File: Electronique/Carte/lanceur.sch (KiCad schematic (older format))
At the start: 4 parts, among them P4 CONN_jacky_led, P5 CONN_LED, Q1 IRF540N, U9 MC34152

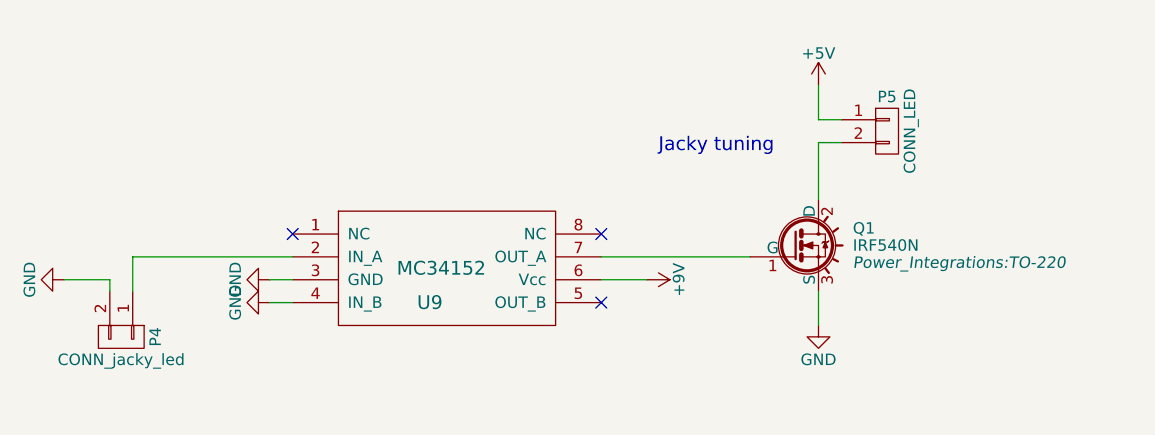
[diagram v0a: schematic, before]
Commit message: rapide corretion des empreintes pour les servos
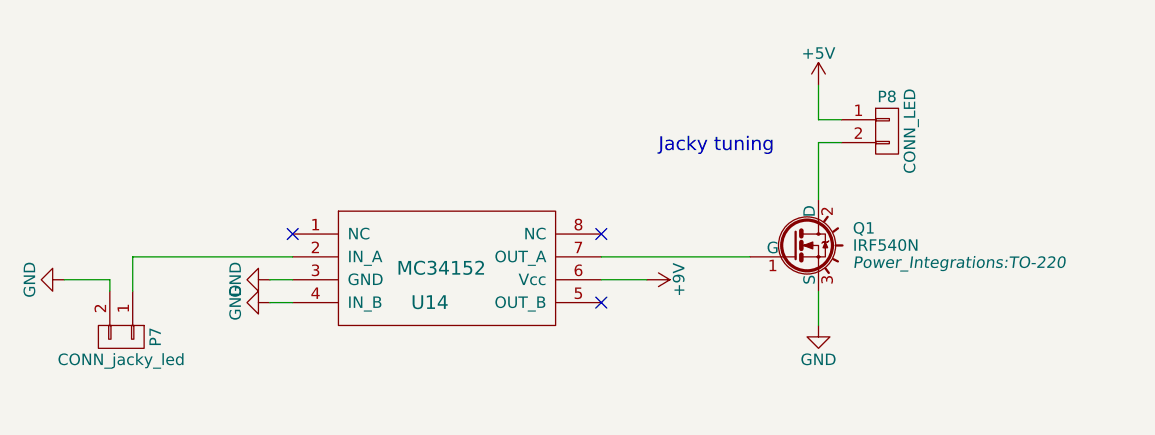
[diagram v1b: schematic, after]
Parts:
- renumbered P4 to P7, P5 to P8, U9 to U14
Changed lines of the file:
@@
 Jacky tuning
 $Comp
-L MC34152 U9
+L MC34152 U14
 U 1 1 5A767332
 P 4600 3900
-F 0 "U9" H 4600 4000 60  0000 C CNN
+F 0 "U14" H 4600 4000 60  0000 C CNN
 F 1 "MC34152" H 4650 4150 60  0000 C CNN
 F 2 "Housings_DIP:DIP-8_W7.62mm_LongPads" H 4600 3900 60  0001 C CNN
@@
 NoConn ~ 5350 3800
 $Comp
-L GND #PWR049
+L GND #PWR26
 U 1 1 5A767FBA
 P 3900 3800
-F 0 "#PWR049" H 3900 3550 50  0001 C CNN
+F 0 "#PWR26" H 3900 3550 50  0001 C CNN
 F 1 "GND" H 3900 3650 50  0000 C CNN
 F 2 "" H 3900 3800 50  0000 C CNN
@@
 $EndComp
 $Comp
-L GND #PWR050
+L GND #PWR25
 U 1 1 5A767FD6
 P 3900 3700
-F 0 "#PWR050" H 3900 3450 50  0001 C CNN
+F 0 "#PWR25" H 3900 3450 50  0001 C CNN
 F 1 "GND" H 3900 3550 50  0000 C CNN
 F 2 "" H 3900 3700 50  0000 C CNN
@@
 	5350 3600 6000 3600
 $Comp
-L CONN_01X02 P4
+L CONN_01X02 P7
 U 1 1 5A76819E
 P 3250 3950
-F 0 "P4" H 3250 4100 50  0000 C CNN
+F 0 "P7" H 3250 4100 50  0000 C CNN
 F 1 "CONN_jacky_led" V 3350 3950 50  0000 C CNN
 F 2 "Connectors_Molex:Molex_KK-6410-02_02x2.54mm_Straight" H 3250 3950 50  0001 C CNN
@@
 	3300 3600 4000 3600
 $Comp
-L GND #PWR051
+L GND #PWR24
 U 1 1 5A768319
 P 3000 3700
-F 0 "#PWR051" H 3000 3450 50  0001 C CNN
+F 0 "#PWR24" H 3000 3450 50  0001 C CNN
 F 1 "GND" H 3000 3550 50  0000 C CNN
 F 2 "" H 3000 3700 50  0000 C CNN
@@
 	3200 3700 3200 3750
 $Comp
-L GND #PWR052
+L GND #PWR29
 U 1 1 5A7685B8
 P 6300 3900
-F 0 "#PWR052" H 6300 3650 50  0001 C CNN
+F 0 "#PWR29" H 6300 3650 50  0001 C CNN
 F 1 "GND" H 6300 3750 50  0000 C CNN
 F 2 "" H 6300 3900 50  0000 C CNN
@@
 	6300 3750 6300 3900
 $Comp
-L CONN_01X02 P5
+L CONN_01X02 P8
 U 1 1 5A76883C
 P 6600 3050
-F 0 "P5" H 6600 3200 50  0000 C CNN
+F 0 "P8" H 6600 3200 50  0000 C CNN
 F 1 "CONN_LED" V 6700 3050 50  0000 C CNN
 F 2 "Connectors_Molex:Molex_KK-6410-02_02x2.54mm_Straight" H 6600 3050 50  0001 C CNN
@@
 $EndComp
 $Comp
-L +5V #PWR053
+L +5V #PWR28
 U 1 1 5A768873
 P 6300 2850
-F 0 "#PWR053" H 6300 2700 50  0001 C CNN
+F 0 "#PWR28" H 6300 2700 50  0001 C CNN
 F 1 "+5V" H 6300 2990 50  0000 C CNN
 F 2 "" H 6300 2850 50  0000 C CNN
@@
 	6300 3100 6300 3350
 $Comp
-L +9V #PWR054
+L +9V #PWR27
 U 1 1 5ABD7B5A
 P 5550 3700
-F 0 "#PWR054" H 5550 3550 50  0001 C CNN
+F 0 "#PWR27" H 5550 3550 50  0001 C CNN
 F 1 "+9V" H 5550 3840 50  0000 C CNN
 F 2 "" H 5550 3700 50  0000 C CNN

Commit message: correction
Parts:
- removed P7: CONN_jacky_led, Connectors_Molex:Molex_KK-6410-02_02x2.54mm_Straight, symbol CONN_01X02
- removed P8: CONN_LED, Connectors_Molex:Molex_KK-6410-02_02x2.54mm_Straight, symbol CONN_01X02
- added D11: D, Diodes_SMD:D_SMA_Handsoldering, symbol D
- added J8: Conn_01x02, dsn2596:B plug 5mm, symbol Conn_01x02
- renumbered U14 to U15
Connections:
- net GND: now also D11.2 (A), J8.1 (Pin_1)
- net at Q1.2 (D): now also D11.1 (K), J8.2 (Pin_2)
- net lanceur: now reaches U15.2 (IN_A)
- net +9V renamed +15V_P
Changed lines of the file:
@@
 Jacky tuning
 $Comp
-L MC34152 U14
+L MC34152 U15
 U 1 1 5A767332
 P 4600 3900
-F 0 "U14" H 4600 4000 60  0000 C CNN
+F 0 "U15" H 4600 4000 60  0000 C CNN
 F 1 "MC34152" H 4650 4150 60  0000 C CNN
 F 2 "Housings_DIP:DIP-8_W7.62mm_LongPads" H 4600 3900 60  0001 C CNN
@@
 NoConn ~ 5350 3800
 $Comp
-L GND #PWR26
+L GND #PWR25
 U 1 1 5A767FBA
 P 3900 3800
-F 0 "#PWR26" H 3900 3550 50  0001 C CNN
+F 0 "#PWR25" H 3900 3550 50  0001 C CNN
 F 1 "GND" H 3900 3650 50  0000 C CNN
 F 2 "" H 3900 3800 50  0000 C CNN
@@
 $EndComp
 $Comp
-L GND #PWR25
+L GND #PWR24
 U 1 1 5A767FD6
 P 3900 3700
-F 0 "#PWR25" H 3900 3450 50  0001 C CNN
+F 0 "#PWR24" H 3900 3450 50  0001 C CNN
 F 1 "GND" H 3900 3550 50  0000 C CNN
 F 2 "" H 3900 3700 50  0000 C CNN
@@
 Wire Wire Line
 	5350 3600 6000 3600
-$Comp
-L CONN_01X02 P7
-U 1 1 5A76819E
-P 3250 3950
-F 0 "P7" H 3250 4100 50  0000 C CNN
-F 1 "CONN_jacky_led" V 3350 3950 50  0000 C CNN
-F 2 "Connectors_Molex:Molex_KK-6410-02_02x2.54mm_Straight" H 3250 3950 50  0001 C CNN
-F 3 "" H 3250 3950 50  0000 C CNN
-	1    3250 3950
-	0    1    1    0
-$EndComp
 Wire Wire Line
 	3300 3750 3300 3600
@@
 	3300 3600 4000 3600
 $Comp
-L GND #PWR24
-U 1 1 5A768319
-P 3000 3700
-F 0 "#PWR24" H 3000 3450 50  0001 C CNN
-F 1 "GND" H 3000 3550 50  0000 C CNN
-F 2 "" H 3000 3700 50  0000 C CNN
-F 3 "" H 3000 3700 50  0000 C CNN
-	1    3000 3700
-	0    1    1    0
-$EndComp
-Wire Wire Line
-	3000 3700 3200 3700
-Wire Wire Line
-	3200 3700 3200 3750
-$Comp
-L GND #PWR29
+L GND #PWR26
 U 1 1 5A7685B8
 P 6300 3900
-F 0 "#PWR29" H 6300 3650 50  0001 C CNN
+F 0 "#PWR26" H 6300 3650 50  0001 C CNN
 F 1 "GND" H 6300 3750 50  0000 C CNN
 F 2 "" H 6300 3900 50  0000 C CNN
@@
 Wire Wire Line
 	6300 3750 6300 3900
-$Comp
-L CONN_01X02 P8
-U 1 1 5A76883C
-P 6600 3050
-F 0 "P8" H 6600 3200 50  0000 C CNN
-F 1 "CONN_LED" V 6700 3050 50  0000 C CNN
-F 2 "Connectors_Molex:Molex_KK-6410-02_02x2.54mm_Straight" H 6600 3050 50  0001 C CNN
-F 3 "" H 6600 3050 50  0000 C CNN
-	1    6600 3050
-	1    0    0    -1
-$EndComp
-$Comp
-L +5V #PWR28
-U 1 1 5A768873
-P 6300 2850
-F 0 "#PWR28" H 6300 2700 50  0001 C CNN
-F 1 "+5V" H 6300 2990 50  0000 C CNN
-F 2 "" H 6300 2850 50  0000 C CNN
-F 3 "" H 6300 2850 50  0000 C CNN
-	1    6300 2850
-	1    0    0    -1
-$EndComp
-Wire Wire Line
-	6300 2850 6300 3000
-Wire Wire Line
-	6300 3000 6400 3000
 Wire Wire Line
 	6400 3100 6300 3100
 Wire Wire Line
 	6300 3100 6300 3350
+Wire Wire Line
+	5350 3700 5550 3700
+Text GLabel 3300 3750 3    60   Input ~ 0
+lanceur
+Text GLabel 5550 3700 2    60   Input ~ 0
++15V_P
 $Comp
-L +9V #PWR27
-U 1 1 5ABD7B5A
-P 5550 3700
-F 0 "#PWR27" H 5550 3550 50  0001 C CNN
-F 1 "+9V" H 5550 3840 50  0000 C CNN
-F 2 "" H 5550 3700 50  0000 C CNN
-F 3 "" H 5550 3700 50  0000 C CNN
-	1    5550 3700
+L Conn_01x02 J8
+U 1 1 5ACAAE5F
+P 6600 3000
+F 0 "J8" H 6600 3100 50  0000 C CNN
+F 1 "Conn_01x02" H 6600 2800 50  0000 C CNN
+F 2 "dsn2596:B plug 5mm" H 6600 3000 50  0001 C CNN
+F 3 "" H 6600 3000 50  0001 C CNN
+	1    6600 3000
+	1    0    0    -1
+$EndComp
+$Comp
+L GND #PWR27
+U 1 1 5ACAAEE8
+P 6400 2650
+F 0 "#PWR27" H 6400 2400 50  0001 C CNN
+F 1 "GND" H 6400 2500 50  0000 C CNN
+F 2 "" H 6400 2650 50  0000 C CNN
+F 3 "" H 6400 2650 50  0000 C CNN
+	1    6400 2650
 	0    1    1    0
 $EndComp
 Wire Wire Line
-	5350 3700 5550 3700
+	6400 2650 6400 3000
+$Comp
+L D D11
+U 1 1 5ACABC03
+P 6300 2950
+F 0 "D11" H 6300 3050 50  0000 C CNN
+F 1 "D" H 6300 2850 50  0000 C CNN
+F 2 "Diodes_SMD:D_SMA_Handsoldering" H 6300 2950 50  0001 C CNN
+F 3 "" H 6300 2950 50  0001 C CNN
+	1    6300 2950
+	0    -1   -1   0
+$EndComp
+Wire Wire Line
+	6300 2800 6400 2800
+Connection ~ 6400 2800
 $EndSCHEMATC

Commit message: Kicad Final enfin !!
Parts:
- renumbered J8 to J10, U15 to U12
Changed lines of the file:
@@
 Jacky tuning
 $Comp
-L MC34152 U15
+L MC34152 U12
 U 1 1 5A767332
 P 4600 3900
-F 0 "U15" H 4600 4000 60  0000 C CNN
+F 0 "U12" H 4600 4000 60  0000 C CNN
 F 1 "MC34152" H 4650 4150 60  0000 C CNN
 F 2 "Housings_DIP:DIP-8_W7.62mm_LongPads" H 4600 3900 60  0001 C CNN
@@
 NoConn ~ 5350 3800
 $Comp
-L GND #PWR25
+L GND #PWR28
 U 1 1 5A767FBA
 P 3900 3800
-F 0 "#PWR25" H 3900 3550 50  0001 C CNN
+F 0 "#PWR28" H 3900 3550 50  0001 C CNN
 F 1 "GND" H 3900 3650 50  0000 C CNN
 F 2 "" H 3900 3800 50  0000 C CNN
@@
 $EndComp
 $Comp
-L GND #PWR24
+L GND #PWR27
 U 1 1 5A767FD6
 P 3900 3700
-F 0 "#PWR24" H 3900 3450 50  0001 C CNN
+F 0 "#PWR27" H 3900 3450 50  0001 C CNN
 F 1 "GND" H 3900 3550 50  0000 C CNN
 F 2 "" H 3900 3700 50  0000 C CNN
@@
 	3300 3600 4000 3600
 $Comp
-L GND #PWR26
+L GND #PWR29
 U 1 1 5A7685B8
 P 6300 3900
-F 0 "#PWR26" H 6300 3650 50  0001 C CNN
+F 0 "#PWR29" H 6300 3650 50  0001 C CNN
 F 1 "GND" H 6300 3750 50  0000 C CNN
 F 2 "" H 6300 3900 50  0000 C CNN
@@
 +15V_P
 $Comp
-L Conn_01x02 J8
+L Conn_01x02 J10
 U 1 1 5ACAAE5F
 P 6600 3000
-F 0 "J8" H 6600 3100 50  0000 C CNN
+F 0 "J10" H 6600 3100 50  0000 C CNN
 F 1 "Conn_01x02" H 6600 2800 50  0000 C CNN
 F 2 "dsn2596:B plug 5mm" H 6600 3000 50  0001 C CNN
@@
 $EndComp
 $Comp
-L GND #PWR27
+L GND #PWR30
 U 1 1 5ACAAEE8
 P 6400 2650
-F 0 "#PWR27" H 6400 2400 50  0001 C CNN
+F 0 "#PWR30" H 6400 2400 50  0001 C CNN
 F 1 "GND" H 6400 2500 50  0000 C CNN
 F 2 "" H 6400 2650 50  0000 C CNN
